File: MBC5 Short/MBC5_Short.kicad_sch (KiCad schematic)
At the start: 4 parts, among them U1 MBM29F033C, U2 MBC5, U3 FM18W08, U99 CartBus

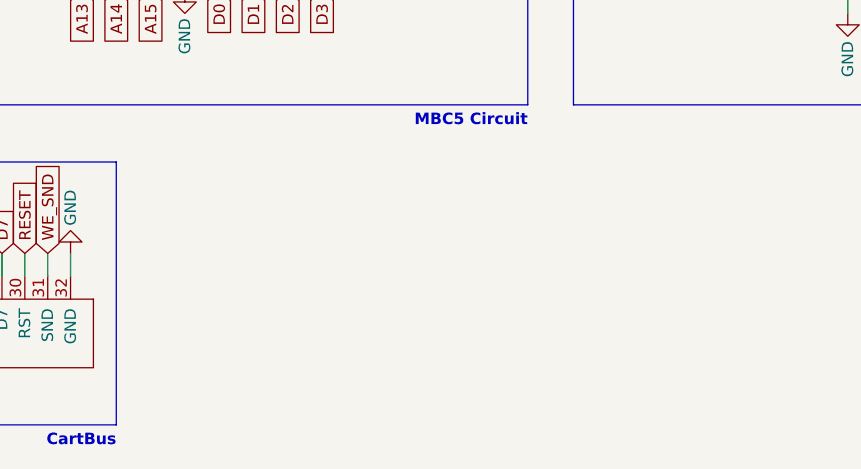
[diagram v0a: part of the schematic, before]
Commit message: Add decoupling capacitors
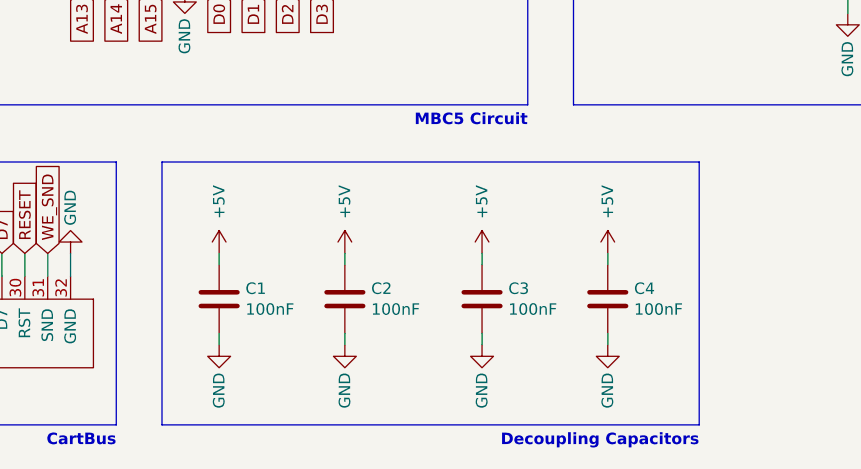
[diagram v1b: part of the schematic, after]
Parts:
- added C1, C2, C3, C4: 100nF, Capacitor_SMD:C_0603_1608Metric, symbol Device:C
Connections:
- net +5V: now also C1.1, C2.1, C3.1, C4.1
- net GND: now also C1.2, C2.2, C3.2, C4.2
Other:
- note added: "Decoupling Capacitors"

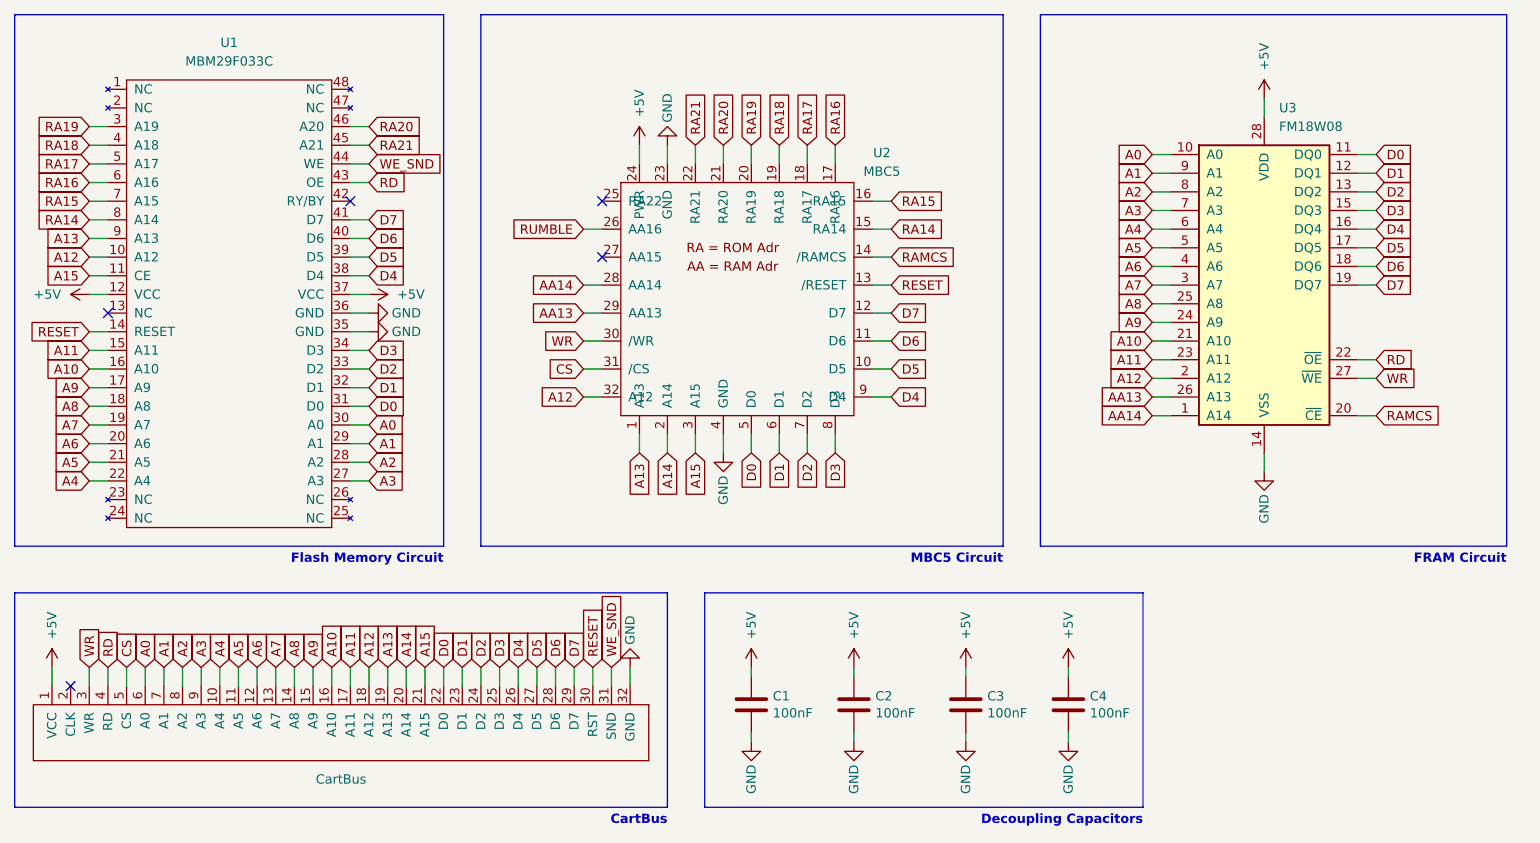
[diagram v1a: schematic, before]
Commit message: Fix 48-pin SOP reference on schemetic with 40-pin footprint package
I changed from the MBM29F033C which I incorrectly had associated with a TSOP-40 and swapped it with the similar AM29F032 package so the pins were all correct.
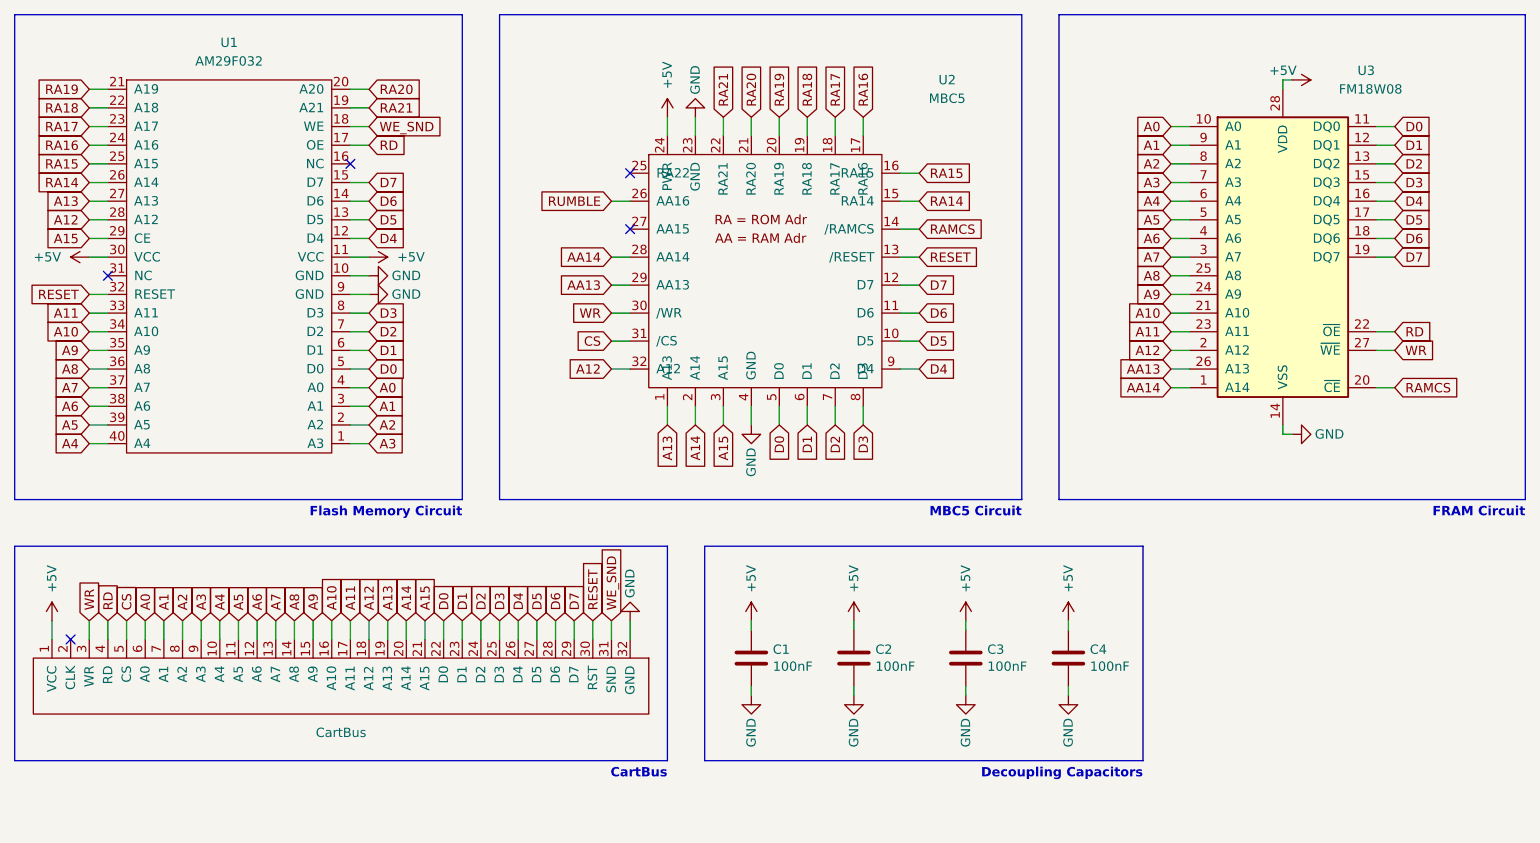
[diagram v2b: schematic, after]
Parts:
- removed U1: MBM29F033C, Package_SO:TSOP-I-40_18.4x10mm_P0.5mm, symbol mbm29f033c:MBM29F033C
- added U1: AM29F032, Package_SO:TSOP-I-40_18.4x10mm_P0.5mm, symbol Gameboy:AM29F032
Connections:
- net +5V: now also U1.11 (VCC~{}), U1.30 (VCC)
- net A0: now also U1.4 (A0~{})
- net A1: now also U1.3 (A1)
- net A10: now also U1.34 (A10)
- net A11: now also U1.33 (A11)
- net A12: now also U1.28 (A12)
- net A13: now also U1.27 (A13)
- net A15: now also U1.29 (CE)
- net A2: now also U1.2 (A2)
- net A3: now also U1.1 (A3)
- net A4: now also U1.40 (A4)
- net A5: now also U1.39 (A5)
- net A6: now also U1.38 (A6)
- net A7: now also U1.37 (A7)
- net A8: now also U1.36 (A8)
- net A9: now also U1.35 (A9)
- net D0: now also U1.5 (D0)
- net D1: now also U1.6 (D1)
- net D2: now also U1.7 (D2)
- net D3: now also U1.8 (D3)
- net D4: now also U1.12 (D4)
- net D5: now also U1.13 (D5)
- net D6: now also U1.14 (D6)
- net D7: now also U1.15 (D7)
- net GND: now also U1.10 (GND), U1.9 (GND)
- net RA14: now also U1.26 (A14)
- net RA15: now also U1.25 (A15)
- net RA16: now also U1.24 (A16)
- net RA17: now also U1.23 (A17)
- net RA18: now also U1.22 (A18)
- net RA19: now also U1.21 (A19)
- net RA20: now also U1.20 (A20)
- net RA21: now also U1.19 (A21)
- net RD: now also U1.17 (OE~{})
- net RESET: now also U1.32 (RESET)
- net WE_SND: now also U1.18 (WE)
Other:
- moved on the sheet: C1, C2, C3, C4, U2, U3
